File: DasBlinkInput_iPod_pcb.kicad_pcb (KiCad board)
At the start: 2 copper layers, 47 x 10.2 mm, 0 parts

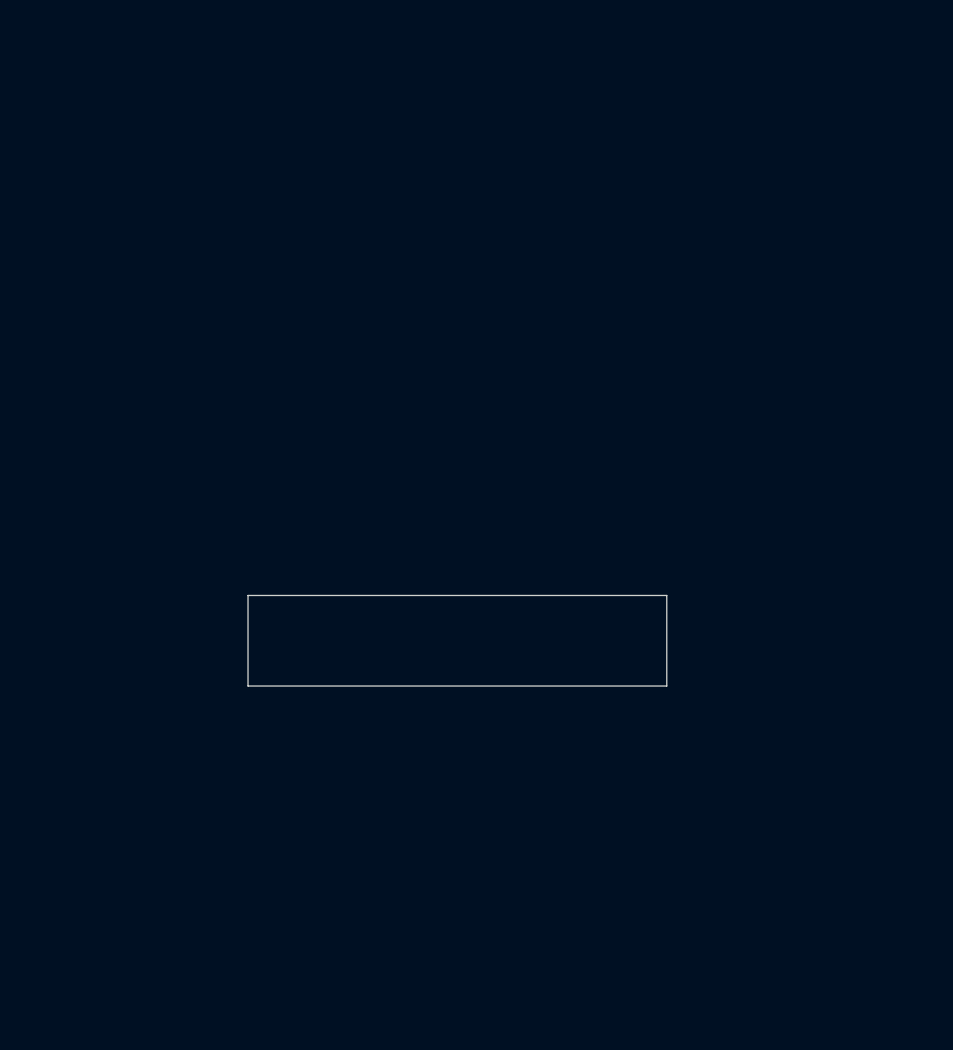
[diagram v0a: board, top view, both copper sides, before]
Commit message: Commencting new layout on corrected iPod defintion
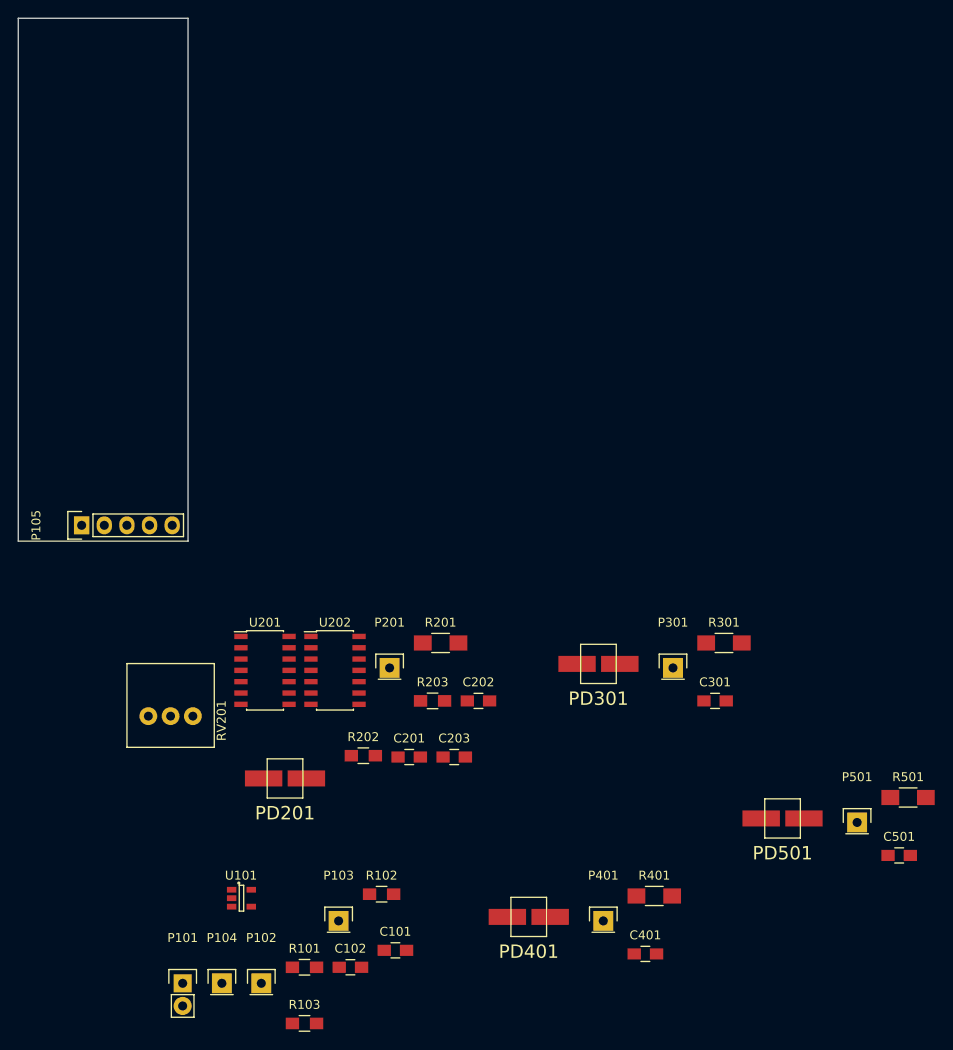
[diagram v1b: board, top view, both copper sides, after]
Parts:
- added C101: 1U, Capacitors_SMD:C_0805_HandSoldering, F.Cu at (110.5, 180.8)
- added C102: 1U, Capacitors_SMD:C_0805_HandSoldering, F.Cu at (105.5, 182.7)
- added C201: 100p, Capacitors_SMD:C_0805_HandSoldering, F.Cu at (112.1, 159.1)
- added C202: 0.1U, Capacitors_SMD:C_0805_HandSoldering, F.Cu at (119.8, 152.8)
- added C203: 0.1U, Capacitors_SMD:C_0805_HandSoldering, F.Cu at (117.1, 159.1)
- added C301: 100p, Capacitors_SMD:C_0805_HandSoldering, F.Cu at (146.4, 152.8)
- added C401: 100p, Capacitors_SMD:C_0805_HandSoldering, F.Cu at (138.6, 181.2)
- added C501: 100p, Capacitors_SMD:C_0805_HandSoldering, F.Cu at (167.0, 170.1)
- added P101: Vin, Pin_Headers:Pin_Header_Straight_1x02, F.Cu at (86.6, 184.5)
- added P102: VGND, Pin_Headers:Pin_Header_Straight_1x01, F.Cu at (95.5, 184.5)
- added P103: 3V, Pin_Headers:Pin_Header_Straight_1x01, F.Cu at (104.1, 177.5)
- added P104: GND, Pin_Headers:Pin_Header_Straight_1x01, F.Cu at (91.0, 184.5)
- added P105: Output, Pin_Headers:Pin_Header_Straight_1x05, F.Cu at (75.3, 133.1)
- added P201: Sig1, Pin_Headers:Pin_Header_Straight_1x01, F.Cu at (109.9, 149.1)
- added P301: Sig2, Pin_Headers:Pin_Header_Straight_1x01, F.Cu at (141.7, 149.1)
- added P401: Sig3, Pin_Headers:Pin_Header_Straight_1x01, F.Cu at (133.8, 177.5)
- added P501: Sig4, Pin_Headers:Pin_Header_Straight_1x01, F.Cu at (162.3, 166.4)
- added PD201: VBPW34SR, DasBlinkInput:VBPW34SR*, F.Cu at (98.1, 161.5)
- added PD301: VBPW34SR, DasBlinkInput:VBPW34SR*, F.Cu at (133.3, 148.7)
- added PD401: VBPW34SR, DasBlinkInput:VBPW34SR*, F.Cu at (125.5, 177.0)
- added PD501: VBPW34SR, DasBlinkInput:VBPW34SR*, F.Cu at (154.0, 166.0)
- added R101: 10K, Resistors_SMD:R_0805_HandSoldering, F.Cu at (100.3, 182.7)
- added R102: 10K, Resistors_SMD:R_0805_HandSoldering, F.Cu at (109.0, 174.5)
- added R103: 0, Resistors_SMD:R_0805_HandSoldering, F.Cu at (100.3, 189.0)
- added R201: 1MEG, Resistors_SMD:R_1206_HandSoldering, F.Cu at (115.6, 146.3)
- added R202: 10K, Resistors_SMD:R_0805_HandSoldering, F.Cu at (106.9, 158.9)
- added R203: 10K, Resistors_SMD:R_0805_HandSoldering, F.Cu at (114.7, 152.8)
- added R301: 1MEG, Resistors_SMD:R_1206_HandSoldering, F.Cu at (147.4, 146.3)
- added R401: 1MEG, Resistors_SMD:R_1206_HandSoldering, F.Cu at (139.6, 174.7)
- added R501: 1MEG, Resistors_SMD:R_1206_HandSoldering, F.Cu at (168.0, 163.6)
- added RV201: POT, DasBlinkInput:P090L-02F25BR10K, F.Cu at (85.3, 154.5)
- added U101: LP2980IM5-3.0/NOPB, Housings_SOT-23_SOT-143_TSOT-6:SOT-23-5, F.Cu at (93.2, 174.9)
- added U201: MCP6404, Housings_SOIC:SOIC-14_3.9x8.7mm_Pitch1.27mm, F.Cu at (95.9, 149.4)
- added U202: LM339, Housings_SOIC:SOIC-14_3.9x8.7mm_Pitch1.27mm, F.Cu at (103.7, 149.4)
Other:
- board size 47 x 10.2 mm -> 19 x 58.7 mm
- board text added: "Device: 4.86" x 2.31" Screen: 1136 x 640 pixel @ 326 ppi 3.48" x 1.963" Board size: 2.13" x 0.75" = 1.7325 In^2"

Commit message: Completed the board layout
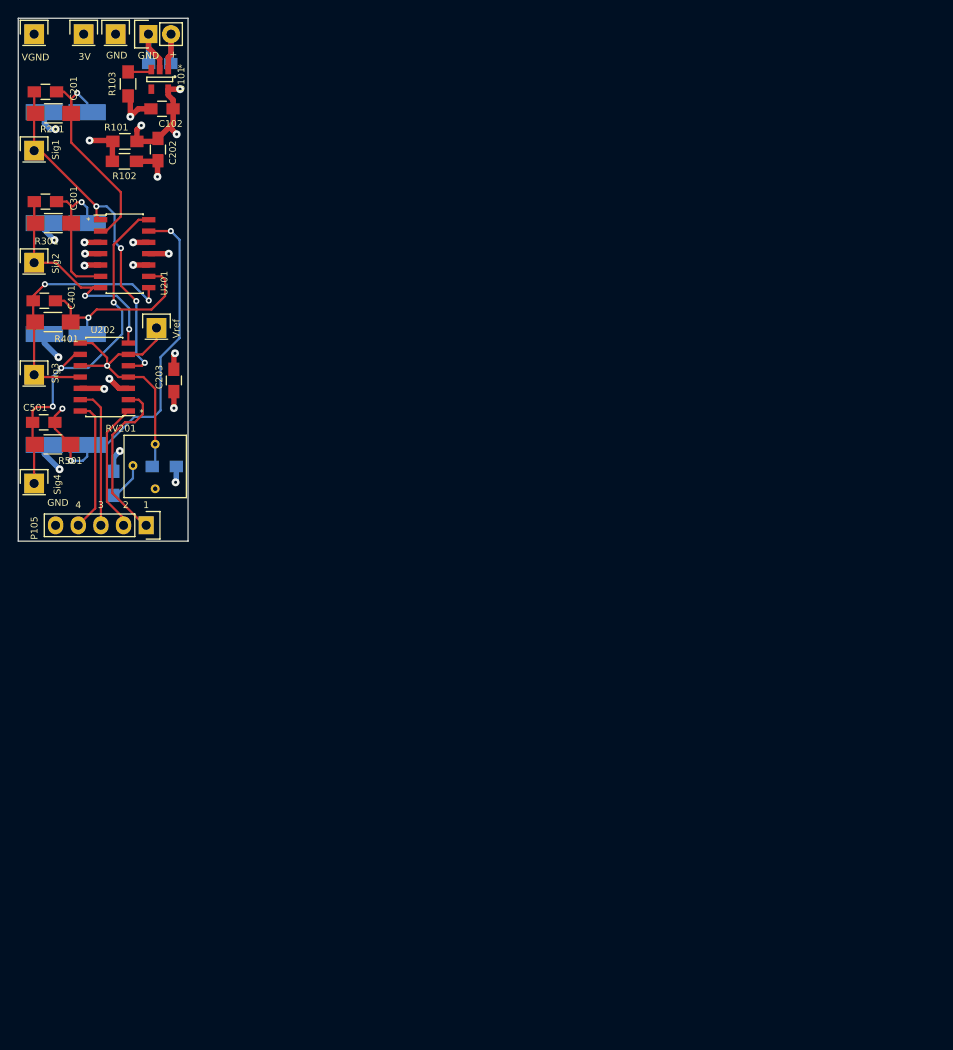
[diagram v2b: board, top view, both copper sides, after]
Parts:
- added P106: Vref, Pin_Headers:Pin_Header_Straight_1x01, F.Cu at (83.7, 110.9)
- C101, PD201, PD301, PD401, PD501, R202, R203: moved to B.Cu
- RV201: footprint DasBlinkInput:P090L-02F25BR10K -> DasBlinkInput:CT6EP
- moved P102 109.5 mm to (70.0, 78.0)
- moved C501 107.6 mm to (71.1, 121.5)
- moved R103 107.3 mm to (80.5, 83.6), turned to 270 degrees
- moved P104 107.2 mm to (79.1, 78.0)
- moved P101 106.6 mm to (82.8, 78.0), turned to 90 degrees
- moved R501 103.8 mm to (72.1, 124.0)
- moved P103 103.5 mm to (75.5, 78.0)
- moved C101 103.0 mm to (84.1, 81.3), turned to 180 degrees
- moved P501 99.9 mm to (70.0, 128.4)
- moved C401 99.6 mm to (71.1, 107.9)
- moved C102 98.6 mm to (84.3, 86.4), turned to 180 degrees
- moved R101 94.8 mm to (80.2, 90.0), turned to 180 degrees
- moved C301 93.7 mm to (71.2, 96.8)
- moved R401 93.3 mm to (72.1, 110.3)
- moved U101 92.3 mm to (84.1, 83.1), turned to 270 degrees
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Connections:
- net /Channel 1 Photodetect/Channel1_Out renamed /Channel 1 Photodetect/PD1
- net /Channel 2 Photodetect/Channel2_Out renamed /Channel 2 Photodetect/PD2
- net /Channel 3 PhotoDetect/Channel3_Out renamed /Channel 3 PhotoDetect/PD3
- net /Channel 4 PhotoDetect/Channel4_Out renamed /Channel 4 PhotoDetect/PD4
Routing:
- net Net-(C501-Pad2): track 0.00 -> 44.6 mm, vias 0 -> 3
- net Net-(C501-Pad1): track 0.00 -> 42.1 mm, vias 0 -> 3
- net Net-(C201-Pad1): track 0.00 -> 40.4 mm, vias 0 -> 4
- net /Channel 2 Photodetect/REF_IN: track 0.00 -> 31.2 mm, vias 0 -> 1
- net Net-(C401-Pad1): track 0.00 -> 29.9 mm, vias 0 -> 2
- net Net-(C301-Pad1): track 0.00 -> 27.1 mm, vias 0 -> 2
- net GND: track 0.00 -> 25.6 mm, vias 0 -> 6
- net Net-(C201-Pad2): track 0.00 -> 25.6 mm, vias 0 -> 1
- net VGND: track 0.00 -> 23.8 mm, vias 0 -> 9
- net 3V: track 0.00 -> 22.3 mm, vias 0 -> 7
- net Net-(C401-Pad2): track 0.00 -> 21.2 mm, vias 0 -> 1
- net /Channel 1 Photodetect/PD1: track 0.00 -> 19.2 mm
- net Net-(C301-Pad2): track 0.00 -> 16.7 mm, vias 0 -> 1
- net /Channel 3 PhotoDetect/PD3: track 0.00 -> 15.9 mm
- net /Channel 4 PhotoDetect/PD4: track 0.00 -> 14.9 mm
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- added copper zone on PWR.Cu, net 3V
- added copper zone on GND.Cu, net GND
- added copper zone on GND.Cu, net VGND
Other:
- copper layers 2 -> 4
- net class Default: clearance 0.2 -> 0.254; trace_width 0.25 -> 0.254; via_dia 0.6 -> 0.6858; via_drill 0.4 -> 0.3302
- net class Power added: clearance 0.254, trace_width 0.6096, via_dia 0.889, via_drill 0.4572
- rule trace_clearance: 0.2 -> 0.254
- rule trace_min: 0.2 -> 0.1524
- rule via_min_drill: 0.3 -> 0.3302
- rule via_min_size: 0.4 -> 0.6858
- board text added: "*"
- board text added: "+"
- board text added: "1"
- board text added: "2"
- board text added: "3"
- board text added: "4"
- board text added: "GND"

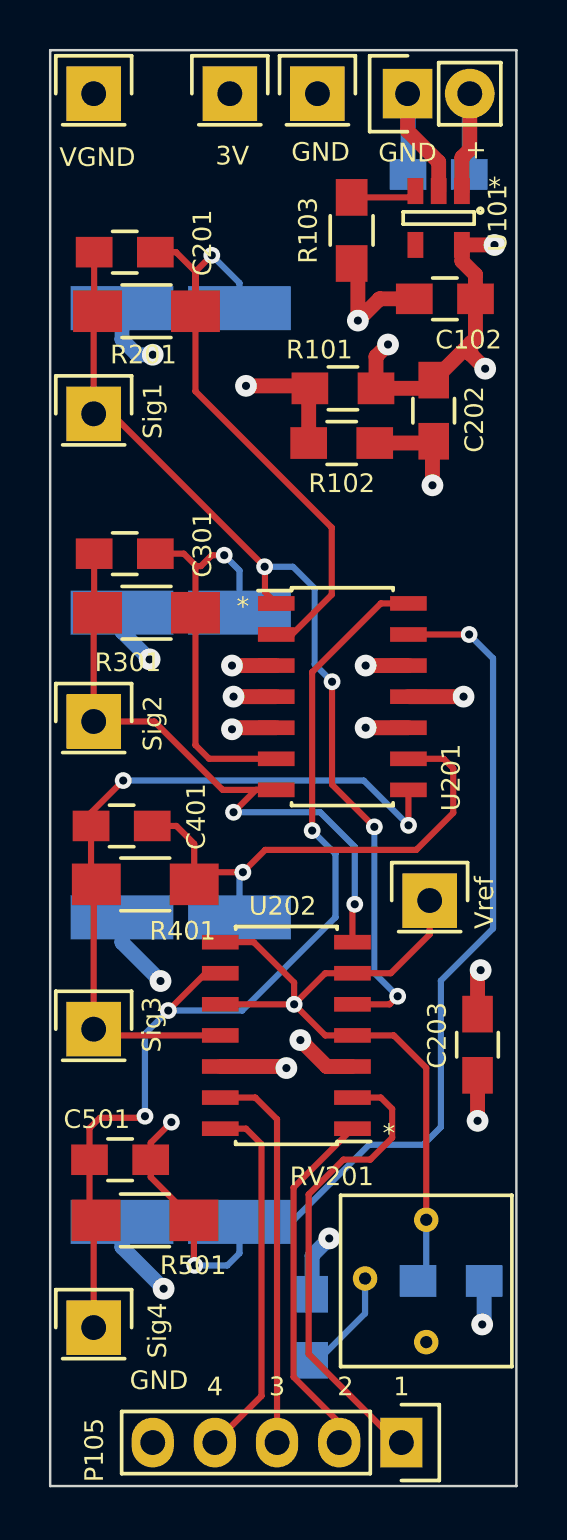
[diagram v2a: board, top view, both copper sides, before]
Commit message: Finalised the board with some logos and generated teh Gerber files
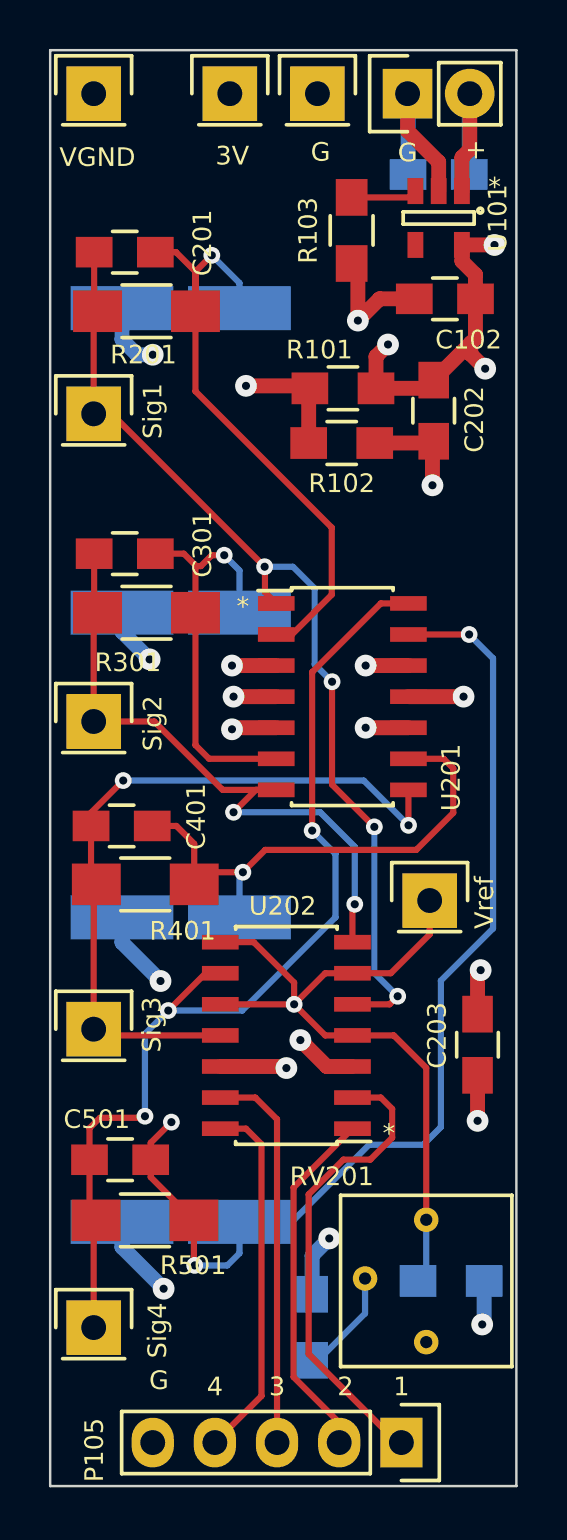
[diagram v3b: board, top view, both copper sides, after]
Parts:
- added G***: LOGO, DasBlinkInput:Logo, B.Cu at (82.3, 104.6)
- added G***: LOGO, DasBlinkInput:kicad_logo, B.Cu at (85.3, 88.3)
- P104: value GND -> G
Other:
- board text added: "Das BlinkInput"
- board text added: "G"
- board text removed: "GND"

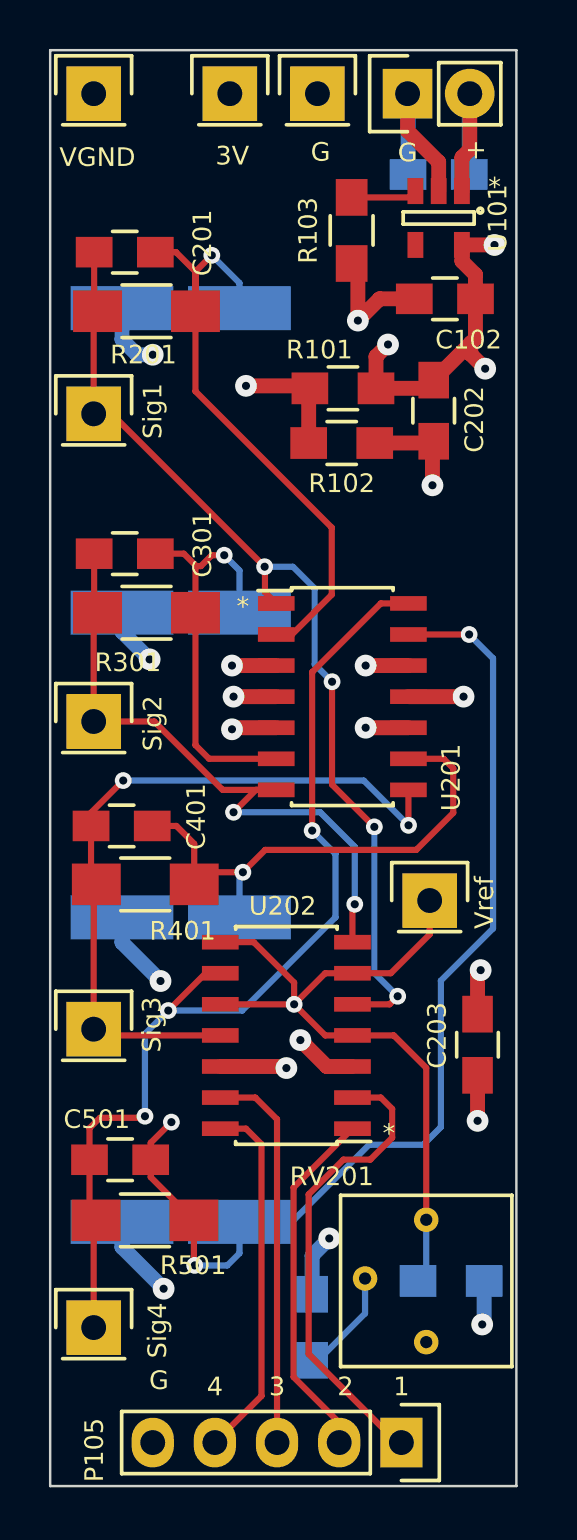
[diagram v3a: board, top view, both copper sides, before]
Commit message: Clean up and correctsion to the layout. Added the pull up resistors
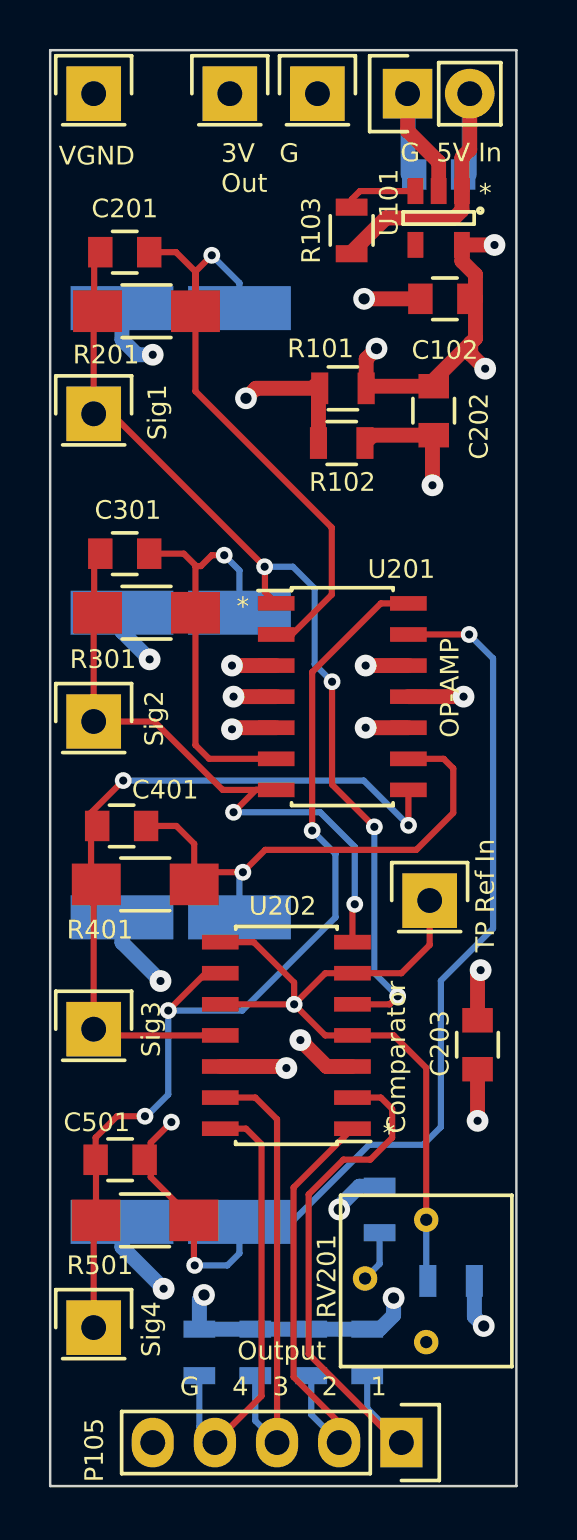
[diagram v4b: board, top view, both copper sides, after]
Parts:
- added R104: 10K, Resistors_SMD:R_0805, B.Cu at (81.2, 129.4)
- added R105: 10K, Resistors_SMD:R_0805, B.Cu at (78.9, 129.4)
- added R106: 10K, Resistors_SMD:R_0805, B.Cu at (76.6, 129.4)
- added R107: 10K, Resistors_SMD:R_0805, B.Cu at (74.3, 129.4)
- C101, C102, C201, C202, C203, C301, C401, C501: footprint Capacitors_SMD:C_0805_HandSoldering -> Capacitors_SMD:C_0805
- P104: value G -> GND
- R101, R102, R103, R202: footprint Resistors_SMD:R_0805_HandSoldering -> Resistors_SMD:R_0805
- R203: value 10K -> 0; footprint Resistors_SMD:R_0805_HandSoldering -> Resistors_SMD:R_0805
- RV201: value POT -> 10K
- moved R203 5.55 mm to (81.7, 123.6)
- moved G*** 0.86 mm to (84.6, 88.8)
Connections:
- R103 pad 2: GND -> Net-(C101-Pad1)
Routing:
- net 3V: track 22.3 -> 32.8 mm, vias 7 -> 9
- net Net-(C101-Pad1): track 7.42 -> 13.5 mm
- net /Channel 1 Photodetect/PD1: track 19.2 -> 22.5 mm
- net /Channel 2 Photodetect/PD2: track 14.6 -> 17.8 mm
- net /Channel 3 PhotoDetect/PD3: track 15.9 -> 19.0 mm
- net /Channel 4 PhotoDetect/PD4: track 14.9 -> 17.9 mm
- net Net-(R203-Pad1): track 4.38 -> 2.12 mm
- net GND: track 25.6 -> 24.1 mm
- net VGND: track 23.8 -> 24.6 mm
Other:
- board text added: "3V G Out"
- board text added: "Comparator"
- board text added: "G 4 3 2 1"
- board text added: "G 5V In"
- board text added: "OP-AMP"
- board text added: "Output"
- board text added: "Sig1"
- board text added: "Sig2"
- board text added: "Sig3"
- board text added: "Sig4"
- board text added: "TP Ref In"
- board text added: "VGND"
- board text removed: "+"
- board text removed: "1"
- board text removed: "2"
- board text removed: "3"
- board text removed: "4"
- board text removed: "G"
